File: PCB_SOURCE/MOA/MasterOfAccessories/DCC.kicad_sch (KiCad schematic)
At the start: 6 parts, among them J901 Screw_Terminal_01x02, U901 6N137

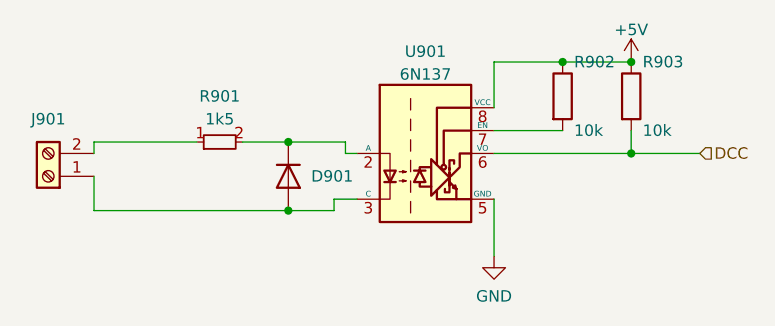
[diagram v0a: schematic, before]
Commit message: fixed bug in ahob program among others
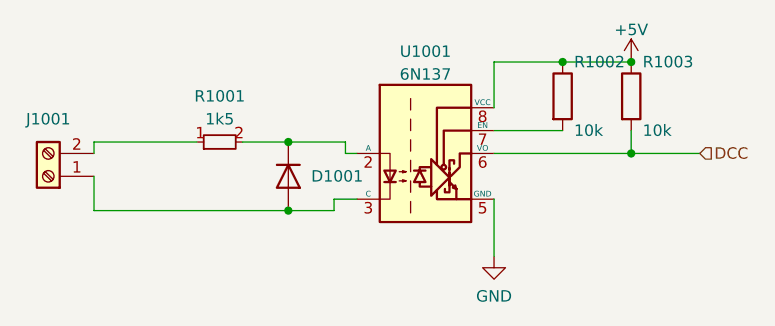
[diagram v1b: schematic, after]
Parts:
- renumbered D901 to D1001, J901 to J1001, R901 to R1001, R902 to R1002, R903 to R1003, U901 to U1001
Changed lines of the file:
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@@
 		(shape input)
 		(at 175.26 92.71 0)
-		(fields_autoplaced yes)
 		(effects
 			(font
@@
 		(dnp no)
 		(fields_autoplaced yes)
-		(property "Reference" "#PWR0901"
+		(property "Reference" "#PWR01001"
 			(at 152.4 110.49 0)
 			(effects
@@
 			(project "MasterOfAccessories"
 				(path "/d28c018f-83ab-41ca-9c80-395a46ff97ad/ed9ef930-f579-4e8b-8cb4-3cc008c01dc5"
-					(reference "#PWR0901")
+					(reference "#PWR01001")
 					(unit 1)
 				)
@@
 			(project "general_schematics"
 				(path "/e777d9ec-d073-4229-a9e6-2cf85636e407/c3ae8e23-d3b7-46ce-84c2-3bde61a5ce74"
-					(reference "#PWR0112")
+					(reference "#PWR?")
 					(unit 1)
 				)
@@
 		(dnp no)
 		(fields_autoplaced yes)
-		(property "Reference" "D901"
+		(property "Reference" "D1001"
 			(at 132.08 95.2499 90)
 			(effects
@@
 			(project "MasterOfAccessories"
 				(path "/d28c018f-83ab-41ca-9c80-395a46ff97ad/ed9ef930-f579-4e8b-8cb4-3cc008c01dc5"
-					(reference "D901")
+					(reference "D1001")
 					(unit 1)
 				)
@@
 		(dnp no)
 		(fields_autoplaced yes)
-		(property "Reference" "#PWR0902"
+		(property "Reference" "#PWR01002"
 			(at 167.64 86.36 0)
 			(effects
@@
 			(project "MasterOfAccessories"
 				(path "/d28c018f-83ab-41ca-9c80-395a46ff97ad/ed9ef930-f579-4e8b-8cb4-3cc008c01dc5"
-					(reference "#PWR0902")
+					(reference "#PWR01002")
 					(unit 1)
 				)
@@
 			(project "general_schematics"
 				(path "/e777d9ec-d073-4229-a9e6-2cf85636e407/c3ae8e23-d3b7-46ce-84c2-3bde61a5ce74"
-					(reference "#PWR0111")
+					(reference "#PWR?")
 					(unit 1)
 				)
@@
 		(dnp no)
 		(fields_autoplaced yes)
-		(property "Reference" "R901"
+		(property "Reference" "R1001"
 			(at 121.92 86.36 90)
 			(effects
@@
 			(project "MasterOfAccessories"
 				(path "/d28c018f-83ab-41ca-9c80-395a46ff97ad/ed9ef930-f579-4e8b-8cb4-3cc008c01dc5"
-					(reference "R901")
+					(reference "R1001")
 					(unit 1)
 				)
@@
 		(dnp no)
 		(fields_autoplaced yes)
-		(property "Reference" "J901"
+		(property "Reference" "J1001"
 			(at 102.87 88.9 0)
 			(effects
@@
 			(project "MasterOfAccessories"
 				(path "/d28c018f-83ab-41ca-9c80-395a46ff97ad/ed9ef930-f579-4e8b-8cb4-3cc008c01dc5"
-					(reference "J901")
+					(reference "J1001")
 					(unit 1)
 				)
@@
 		(on_board yes)
 		(dnp no)
-		(property "Reference" "R902"
+		(property "Reference" "R1002"
 			(at 161.29 82.55 0)
 			(effects
@@
 			(project "MasterOfAccessories"
 				(path "/d28c018f-83ab-41ca-9c80-395a46ff97ad/ed9ef930-f579-4e8b-8cb4-3cc008c01dc5"
-					(reference "R902")
+					(reference "R1002")
 					(unit 1)
 				)
@@
 			(project "general_schematics"
 				(path "/e777d9ec-d073-4229-a9e6-2cf85636e407/c3ae8e23-d3b7-46ce-84c2-3bde61a5ce74"
-					(reference "R702")
+					(reference "R?")
 					(unit 1)
 				)
@@
 		(on_board yes)
 		(dnp no)
-		(property "Reference" "R903"
+		(property "Reference" "R1003"
 			(at 168.91 82.55 0)
 			(effects
@@
 			(project "MasterOfAccessories"
 				(path "/d28c018f-83ab-41ca-9c80-395a46ff97ad/ed9ef930-f579-4e8b-8cb4-3cc008c01dc5"
-					(reference "R903")
+					(reference "R1003")
 					(unit 1)
 				)
@@
 			(project "general_schematics"
 				(path "/e777d9ec-d073-4229-a9e6-2cf85636e407/c3ae8e23-d3b7-46ce-84c2-3bde61a5ce74"
-					(reference "R703")
+					(reference "R?")
 					(unit 1)
 				)
@@
 		(dnp no)
 		(fields_autoplaced yes)
-		(property "Reference" "U901"
+		(property "Reference" "U1001"
 			(at 144.78 81.3902 0)
 			(effects
@@
 			(project "MasterOfAccessories"
 				(path "/d28c018f-83ab-41ca-9c80-395a46ff97ad/ed9ef930-f579-4e8b-8cb4-3cc008c01dc5"
-					(reference "U901")
+					(reference "U1001")
 					(unit 1)
 				)
@@
 			(project "general_schematics"
 				(path "/e777d9ec-d073-4229-a9e6-2cf85636e407/c3ae8e23-d3b7-46ce-84c2-3bde61a5ce74"
-					(reference "U701")
-					(unit 1)
-				)
+					(reference "U?")
+					(unit 1)
+				)
